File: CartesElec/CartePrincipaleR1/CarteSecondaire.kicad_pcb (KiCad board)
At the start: 2 copper layers, 40 parts, among them J10 SERVO2, J14 Screw_Terminal_01x02, J15 MOT_PWM_2, J16 MOT_PWM_1, J17 SERVO1, J18 Conn_02x08_Top_Bottom, J19 ENC_FOL_1, J20 ENC_MOT_1, J21 ENC_FOL_2, J22 ENC_MOT_2, J23 AX12_1, J24 AX12_2, J7 Conn_02x08_Top_Bottom, J9 SERVO3, Q1 IRLML0030, Q2 IRLML0030, Q3 IRLML0030, Q4 IRLML0030, U3 TSR_1-2450

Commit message: secondaire update
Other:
- board outline added: 52 x 66 mm
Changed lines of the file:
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@@
     )
   )
+  (gr_rect (start 78 119) (end 130 185) (layer "Edge.Cuts") (width 0.05) (fill none))
   (segment (start 85.09 139.7) (end 86.36 139.7) (width 1.2) (layer "F.Cu") (net 1))
   (segment (start 82.55 137.16) (end 82.55 133.48) (width 1.2) (layer "F.Cu") (net 1))

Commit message: error fix
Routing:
- net S1: track 14.7 -> 14.5 mm, vias 1 -> 0
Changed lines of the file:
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@@
     (pad "" np_thru_hole circle (at 0 0) (size 3.2 3.2) (drill 3.2) (layers *.Cu *.Mask))
   )
-  (footprint "Connector_IDC:IDC-Header_2x08_P2.54mm_Vertical" (layer "F.Cu")
+  (footprint "Connector_IDC:IDC-Header_2x08_P2.54mm_Vertical" locked (layer "F.Cu")
     (at 102.87 143.51 180)
     (descr "Through hole IDC box header, 2x08, 2.54mm pitch, DIN 41651 / IEC 60603-13, double rows, https://docs.google.com/spreadsheets/d/16SsEcesNF15N3Lb4niX7dcUr-NY5_MFPQhobNuNppn4/edit#gid=0")
@@
     (fp_line (start -1.98 10.94) (end -1.98 10.94) (layer "F.Fab") (width 0.1))
     (fp_line (start -1.98 6.84) (end -1.98 -3.91) (layer "F.Fab") (width 0.1))
-    (pad "1" thru_hole roundrect (at 0 0 180) (size 1.7 1.7) (drill 1) (layers *.Cu *.Mask) (roundrect_rratio 0.147059)
+    (pad "1" thru_hole roundrect locked (at 0 0 180) (size 1.7 1.7) (drill 1) (layers *.Cu *.Mask) (roundrect_rratio 0.147059)
       (net 2 "GND") (pinfunction "Pin_1") (pintype "passive"))
-    (pad "2" thru_hole circle (at 2.54 0 180) (size 1.7 1.7) (drill 1) (layers *.Cu *.Mask)
+    (pad "2" thru_hole circle locked (at 2.54 0 180) (size 1.7 1.7) (drill 1) (layers *.Cu *.Mask)
       (net 2 "GND") (pinfunction "Pin_2") (pintype "passive"))
-    (pad "3" thru_hole circle (at 0 2.54 180) (size 1.7 1.7) (drill 1) (layers *.Cu *.Mask)
+    (pad "3" thru_hole circle locked (at 0 2.54 180) (size 1.7 1.7) (drill 1) (layers *.Cu *.Mask)
       (net 3 "+5V") (pinfunction "Pin_3") (pintype "passive"))
-    (pad "4" thru_hole circle (at 2.54 2.54 180) (size 1.7 1.7) (drill 1) (layers *.Cu *.Mask)
+    (pad "4" thru_hole circle locked (at 2.54 2.54 180) (size 1.7 1.7) (drill 1) (layers *.Cu *.Mask)
       (net 3 "+5V") (pinfunction "Pin_4") (pintype "passive"))
-    (pad "5" thru_hole circle (at 0 5.08 180) (size 1.7 1.7) (drill 1) (layers *.Cu *.Mask)
+    (pad "5" thru_hole circle locked (at 0 5.08 180) (size 1.7 1.7) (drill 1) (layers *.Cu *.Mask)
       (net 23 "Mot2DIR") (pinfunction "Pin_5") (pintype "passive"))
-    (pad "6" thru_hole circle (at 2.54 5.08 180) (size 1.7 1.7) (drill 1) (layers *.Cu *.Mask)
+    (pad "6" thru_hole circle locked (at 2.54 5.08 180) (size 1.7 1.7) (drill 1) (layers *.Cu *.Mask)
       (net 22 "Mot2PWM") (pinfunction "Pin_6") (pintype "passive"))
-    (pad "7" thru_hole circle (at 0 7.62 180) (size 1.7 1.7) (drill 1) (layers *.Cu *.Mask)
+    (pad "7" thru_hole circle locked (at 0 7.62 180) (size 1.7 1.7) (drill 1) (layers *.Cu *.Mask)
       (net 25 "Mot1DIR") (pinfunction "Pin_7") (pintype "passive"))
-    (pad "8" thru_hole circle (at 2.54 7.62 180) (size 1.7 1.7) (drill 1) (layers *.Cu *.Mask)
+    (pad "8" thru_hole circle locked (at 2.54 7.62 180) (size 1.7 1.7) (drill 1) (layers *.Cu *.Mask)
       (net 24 "Mot1PWM") (pinfunction "Pin_8") (pintype "passive"))
-    (pad "9" thru_hole circle (at 0 10.16 180) (size 1.7 1.7) (drill 1) (layers *.Cu *.Mask)
+    (pad "9" thru_hole circle locked (at 0 10.16 180) (size 1.7 1.7) (drill 1) (layers *.Cu *.Mask)
       (net 28 "POMPE2") (pinfunction "Pin_9") (pintype "passive"))
-    (pad "10" thru_hole circle (at 2.54 10.16 180) (size 1.7 1.7) (drill 1) (layers *.Cu *.Mask)
+    (pad "10" thru_hole circle locked (at 2.54 10.16 180) (size 1.7 1.7) (drill 1) (layers *.Cu *.Mask)
       (net 27 "POMPE1") (pinfunction "Pin_10") (pintype "passive"))
-    (pad "11" thru_hole circle (at 0 12.7 180) (size 1.7 1.7) (drill 1) (layers *.Cu *.Mask)
+    (pad "11" thru_hole circle locked (at 0 12.7 180) (size 1.7 1.7) (drill 1) (layers *.Cu *.Mask)
       (net 30 "EV2") (pinfunction "Pin_11") (pintype "passive"))
-    (pad "12" thru_hole circle (at 2.54 12.7 180) (size 1.7 1.7) (drill 1) (layers *.Cu *.Mask)
+    (pad "12" thru_hole circle locked (at 2.54 12.7 180) (size 1.7 1.7) (drill 1) (layers *.Cu *.Mask)
       (net 29 "EV1") (pinfunction "Pin_12") (pintype "passive"))
-    (pad "13" thru_hole circle (at 0 15.24 180) (size 1.7 1.7) (drill 1) (layers *.Cu *.Mask)
+    (pad "13" thru_hole circle locked (at 0 15.24 180) (size 1.7 1.7) (drill 1) (layers *.Cu *.Mask)
       (net 26 "S1") (pinfunction "Pin_13") (pintype "passive"))
-    (pad "14" thru_hole circle (at 2.54 15.24 180) (size 1.7 1.7) (drill 1) (layers *.Cu *.Mask)
+    (pad "14" thru_hole circle locked (at 2.54 15.24 180) (size 1.7 1.7) (drill 1) (layers *.Cu *.Mask)
       (net 21 "S2") (pinfunction "Pin_14") (pintype "passive"))
-    (pad "15" thru_hole circle (at 0 17.78 180) (size 1.7 1.7) (drill 1) (layers *.Cu *.Mask)
+    (pad "15" thru_hole circle locked (at 0 17.78 180) (size 1.7 1.7) (drill 1) (layers *.Cu *.Mask)
       (net 20 "S3") (pinfunction "Pin_15") (pintype "passive"))
-    (pad "16" thru_hole circle (at 2.54 17.78 180) (size 1.7 1.7) (drill 1) (layers *.Cu *.Mask)
+    (pad "16" thru_hole circle locked (at 2.54 17.78 180) (size 1.7 1.7) (drill 1) (layers *.Cu *.Mask)
       (net 31 "+3V3") (pinfunction "Pin_16") (pintype "passive"))
     (model "${KICAD6_3DMODEL_DIR}/Connector_IDC.3dshapes/IDC-Header_2x08_P2.54mm_Vertical.wrl"
@@
   (segment (start 87.63 154.32) (end 88.70763 154.32) (width 0.6) (layer "B.Cu") (net 25))
   (segment (start 115.57 128.27) (end 116.84 127) (width 0.4) (layer "F.Cu") (net 26))
-  (segment (start 102.87 128.46998) (end 102.87 128.27) (width 0.4) (layer "F.Cu") (net 26))
   (segment (start 102.87 128.27) (end 115.57 128.27) (width 0.4) (layer "F.Cu") (net 26))
-  (via (at 102.87 128.46998) (size 0.8) (drill 0.4) (layers "F.Cu" "B.Cu") (net 26))
   (segment (start 94.93 140.0325) (end 94.93 136.21) (width 1.2) (layer "F.Cu") (net 27))
   (segment (start 100.33 133.35) (end 97.79 133.35) (width 1.2) (layer "F.Cu") (net 27))

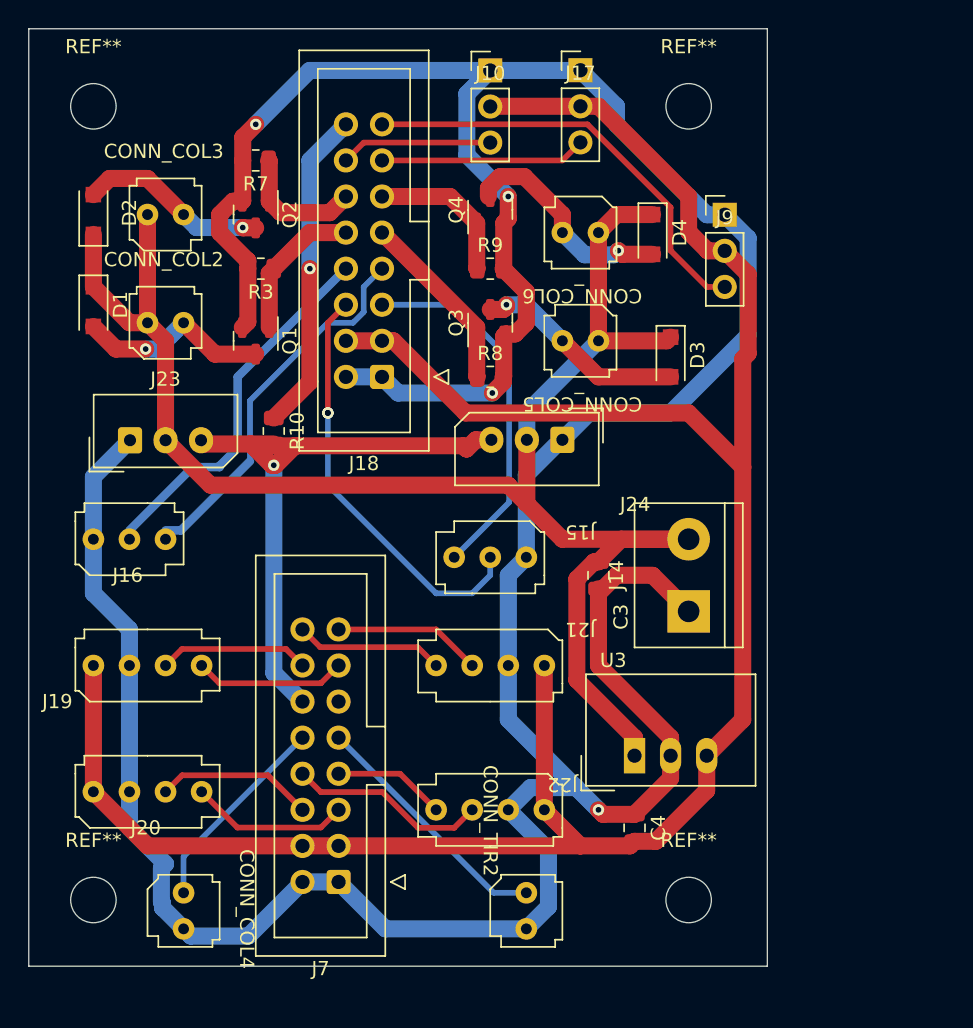
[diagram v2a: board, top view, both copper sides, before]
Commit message: footprint fixes
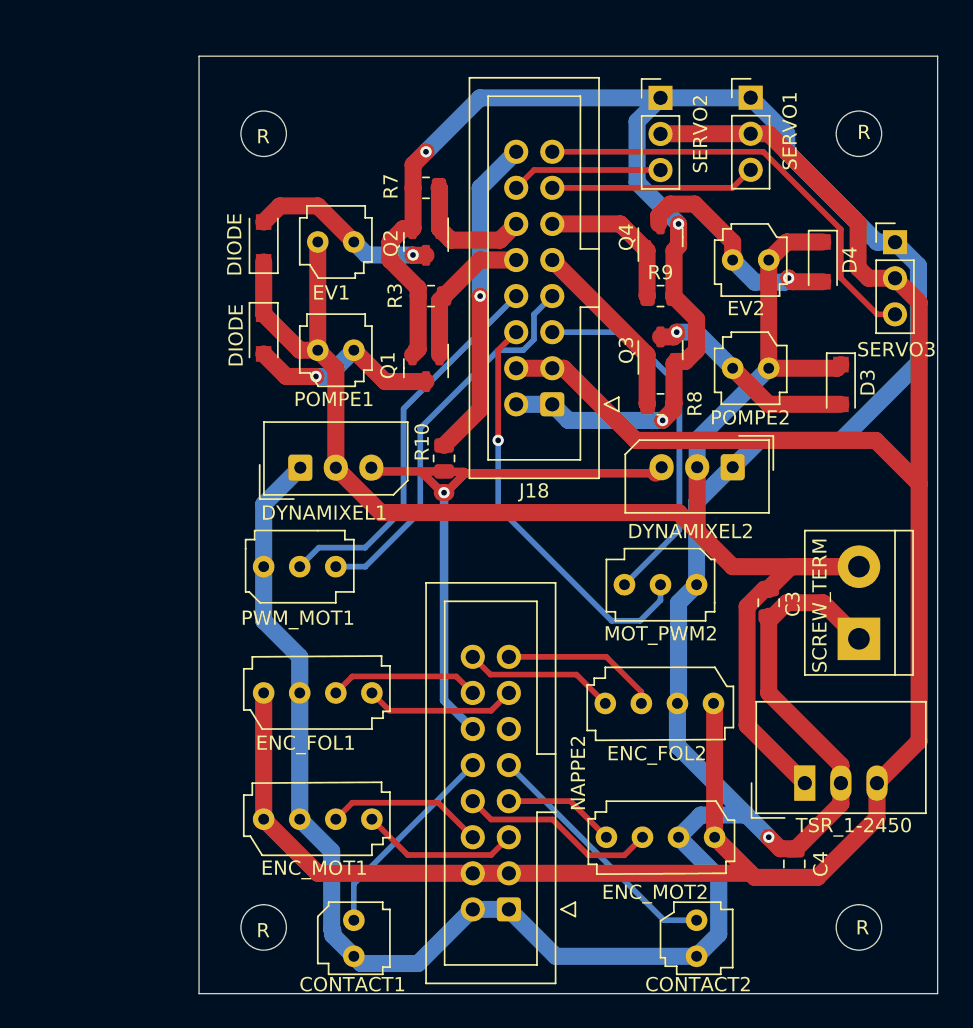
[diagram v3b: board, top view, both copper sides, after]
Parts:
- moved ENC_FOL2 12.2 mm to (126.2, 166.5)
- moved R 12.1 mm to (136.4, 126.4)
- moved R 12.1 mm to (136.4, 182.3)
- moved SCREW_TERM 12.1 mm to (136.4, 162.0)
- moved CONTACT2 12.1 mm to (125.0, 181.0)
- moved D3 12.1 mm to (135.2, 144.0)
- moved DIODE 12.1 mm to (94.5, 140.5)
- moved DIODE 12.1 mm to (94.5, 134.0)
- moved DYNAMIXEL1 12.1 mm to (97.1, 149.9)
- moved DYNAMIXEL2 12.1 mm to (127.6, 149.9)
- moved ENC_FOL1 12.1 mm to (94.5, 165.8)
- moved ENC_MOT1 12.1 mm to (94.5, 174.7)
- moved ENC_MOT2 12.1 mm to (126.3, 175.9)
- moved EV1 12.1 mm to (97.6, 134.0)
- moved MOT_PWM2 12.1 mm to (125.0, 158.1)
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- renumbered CONN_COL4 to CONTACT1, CONN_TIR2 to CONTACT2, D1 to DIODE, D2 to DIODE, J23 to DYNAMIXEL1, J24 to DYNAMIXEL2, J19 to ENC_FOL1, J21 to ENC_FOL2, J20 to ENC_MOT1, J22 to ENC_MOT2, CONN_COL3 to EV1, CONN_COL6 to EV2, J15 to MOT_PWM2, J7 to NAPPE2, CONN_COL2 to POMPE1, CONN_COL5 to POMPE2, J16 to PWM_MOT1, REF** to R, J14 to SCREW_TERM, J17 to SERVO1, J10 to SERVO2, J9 to SERVO3, U3 to TSR_1-2450
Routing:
- net Mot1PWM: track 25.8 -> 27.3 mm
- net Mot1DIR: track 26.4 -> 27.6 mm
- net RC_2A: track 10.5 -> 11.2 mm
- net Mot2PWM: track 29.6 -> 29.3 mm, vias 2 -> 1

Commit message: update PCB masse
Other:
- board text added: "12V"
- board text added: "GND"
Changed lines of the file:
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@@
     (property "Sheetname" "")
     (attr through_hole)
-    (fp_text reference "DYNAMIXEL2" (at 2.959011 -4.528489) (layer "F.SilkS")
+    (fp_text reference "DYNAMIXEL2" (at 2.959011 -4.228489) (layer "F.SilkS")
       (effects (font (size 1 1) (thickness 0.15)))
     )
@@
     )
   )
+  (gr_line (start 124.8 155.45) (end 124.8 154.9) (layer "F.SilkS") (width 0.12))
+  (gr_line (start 122.1 184.2) (end 116.9 184.3) (layer "F.SilkS") (width 0.12))
+  (gr_line (start 116.9 184.3) (end 115.7 182.8) (layer "F.SilkS") (width 0.12))
+  (gr_line (start 133.1 176.7) (end 133.8 176.7) (layer "F.SilkS") (width 0.12))
+  (gr_line (start 104.2 136.1) (end 105.2 136.1) (layer "F.SilkS") (width 0.12))
+  (gr_line (start 127.8 147.6) (end 127.8 147.1) (layer "F.SilkS") (width 0.12))
+  (gr_line (start 96.2 162.7) (end 95.6 161.5) (layer "F.SilkS") (width 0.12))
+  (gr_line (start 105 127.1) (end 104.9 128.7) (layer "F.SilkS") (width 0.12))
+  (gr_line (start 97.1 146.125) (end 97.1 145.475) (layer "F.SilkS") (width 0.12))
+  (gr_line (start 105.1 131.9) (end 104.2 131.9) (layer "F.SilkS") (width 0.12))
+  (gr_line (start 105.3 184.5) (end 104 184.6) (layer "F.SilkS") (width 0.12))
+  (gr_line (start 123.9 135.9) (end 123.9 136.7) (layer "F.SilkS") (width 0.12))
+  (gr_line (start 131 184.3) (end 127.9 184.3) (layer "F.SilkS") (width 0.12))
+  (gr_line (start 105 131.2) (end 105 131.9) (layer "F.SilkS") (width 0.12))
+  (gr_line (start 123.5 143.7) (end 123.5 144.3) (layer "F.SilkS") (width 0.12))
+  (gr_line (start 105.2 136.1) (end 105.2 136.7) (layer "F.SilkS") (width 0.12))
+  (gr_line (start 135.2 178.1) (end 135.2 176.3) (layer "F.SilkS") (width 0.12))
+  (gr_line (start 104.2 131.9) (end 104.2 136.1) (layer "F.SilkS") (width 0.12))
+  (gr_line (start 105.3 139.3) (end 105.3 140.6) (layer "F.SilkS") (width 0.12))
+  (gr_line (start 97.1 171.9) (end 97.1 170.5) (layer "F.SilkS") (width 0.12))
+  (gr_line (start 133.8 176.7) (end 134.2 176.7) (layer "F.SilkS") (width 0.12))
+  (gr_line (start 123.7 171.1) (end 123.7 173) (layer "F.SilkS") (width 0.12))
+  (gr_line (start 126.7 123.1) (end 124.5 123.1) (layer "F.SilkS") (width 0.12))
+  (gr_line (start 141.9 134.1) (end 141 134.1) (layer "F.SilkS") (width 0.12))
   (gr_rect locked (start 89.989011 120.931511) (end 141.989011 186.931511) (layer "Edge.Cuts") (width 0.05) (fill none))
+  (gr_text "12V" (at 136.3 152.9 180) (layer "F.SilkS")
+    (effects (font (size 1 1) (thickness 0.15)))
+  )
+  (gr_text "GND" (at 136.3 165.4) (layer "F.SilkS")
+    (effects (font (size 1 1) (thickness 0.15)))
+  )
   (segment locked (start 97.079011 141.631511) (end 98.349011 141.631511) (width 1.2) (layer "F.Cu") (net 1))
   (segment locked (start 94.539011 139.091511) (end 94.539011 135.411511) (width 1.2) (layer "F.Cu") (net 1))
